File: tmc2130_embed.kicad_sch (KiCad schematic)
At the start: 13 parts, among them U5 TMC2130-LA

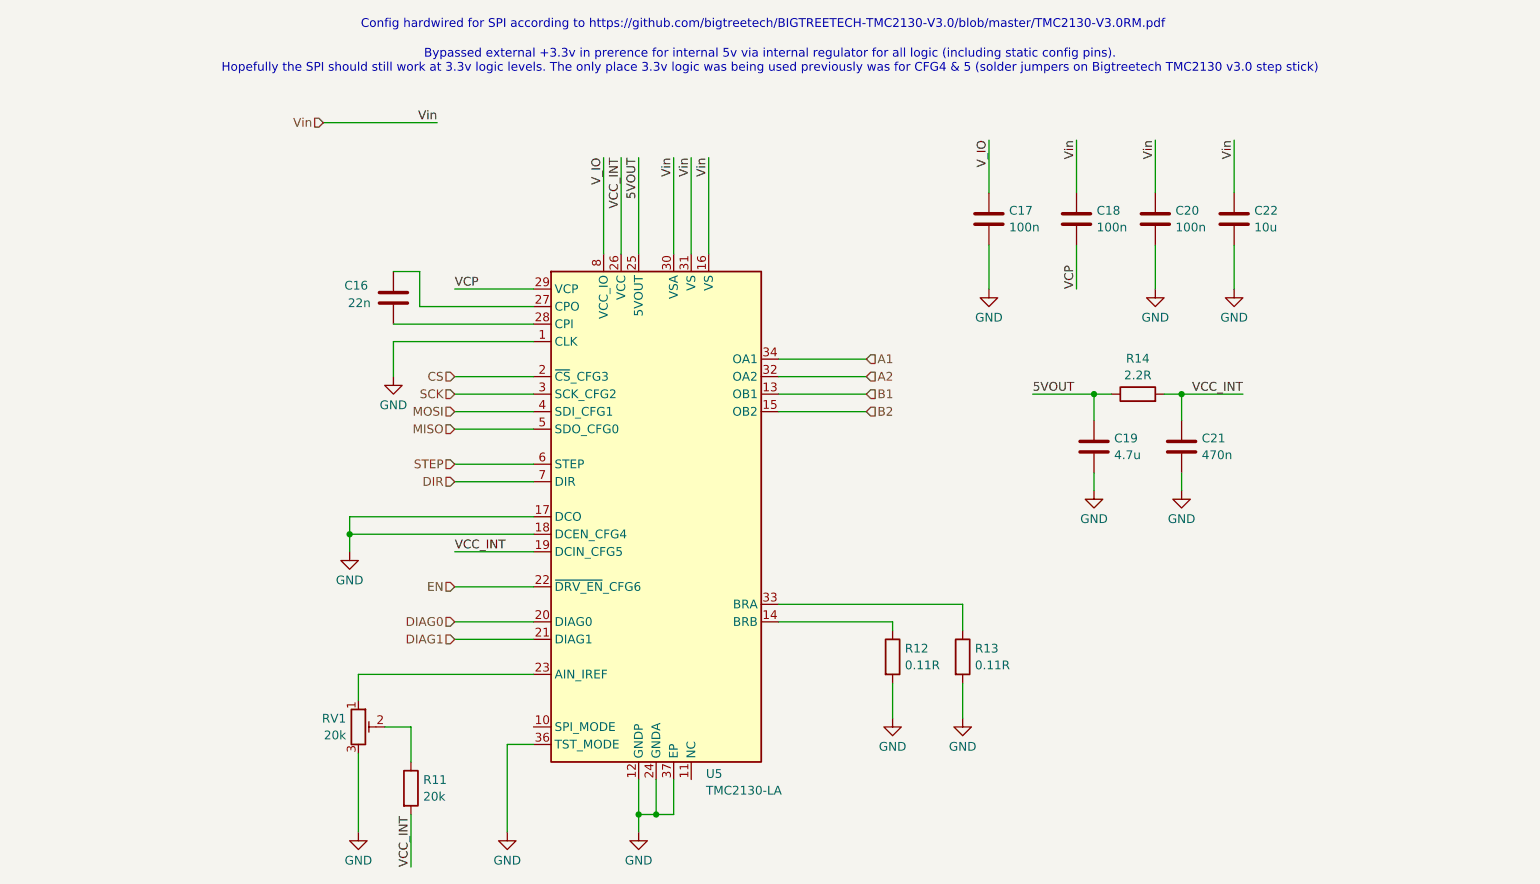
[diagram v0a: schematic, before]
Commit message: Might as well add a z motor stepper driver at this stage
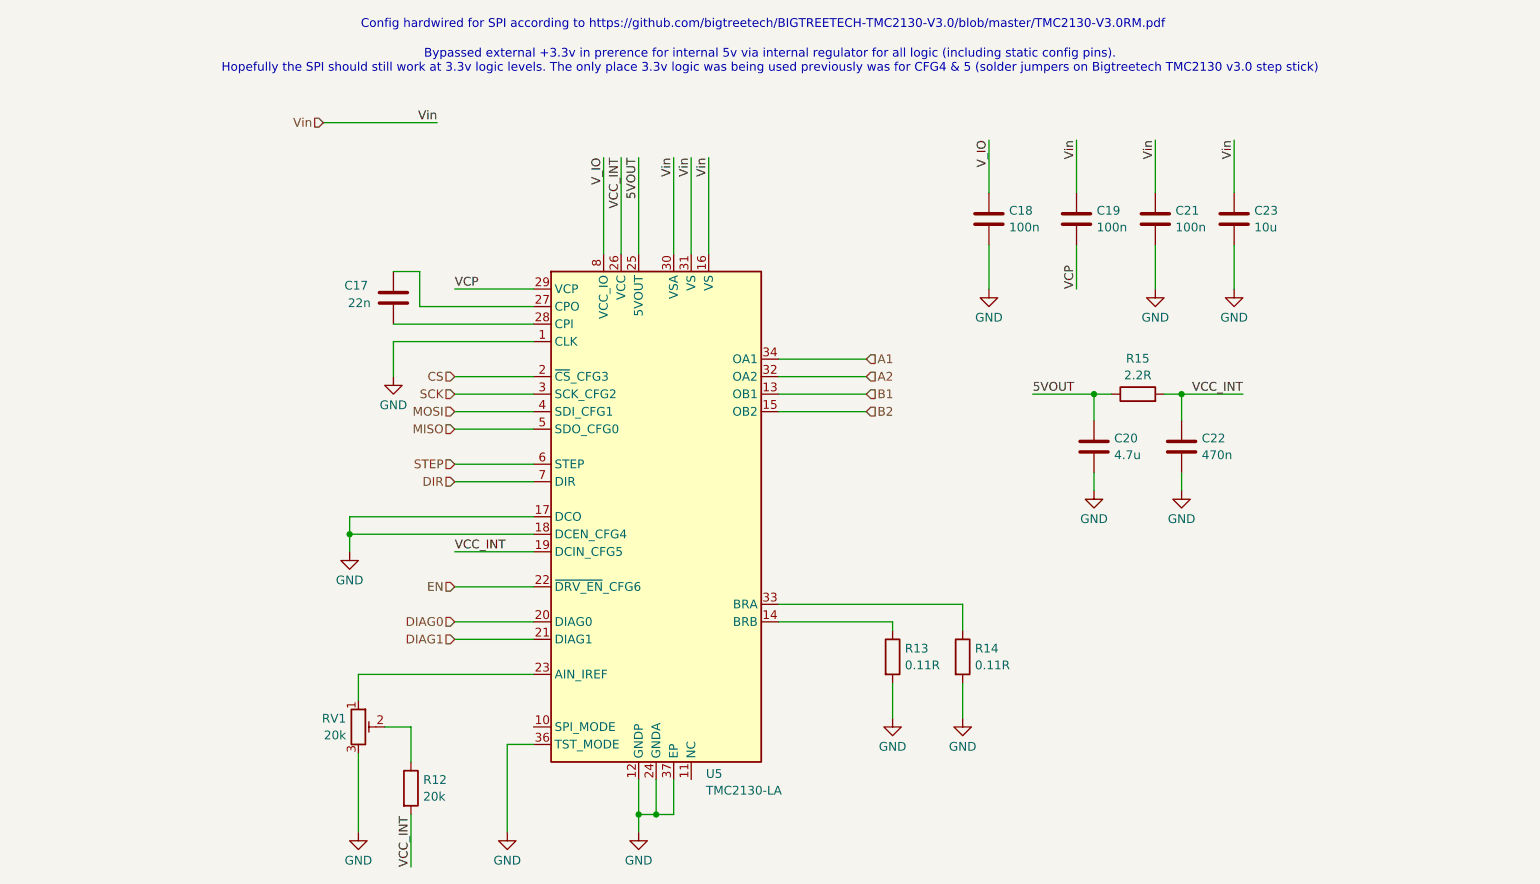
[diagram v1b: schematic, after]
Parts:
- renumbered C16 to C17, C17 to C18, C18 to C19, C19 to C20, C20 to C21, C21 to C22, C22 to C23, R11 to R12, R12 to R13, R13 to R14, R14 to R15
